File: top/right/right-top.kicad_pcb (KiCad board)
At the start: 2 copper layers, 171 x 95 mm, 39 parts

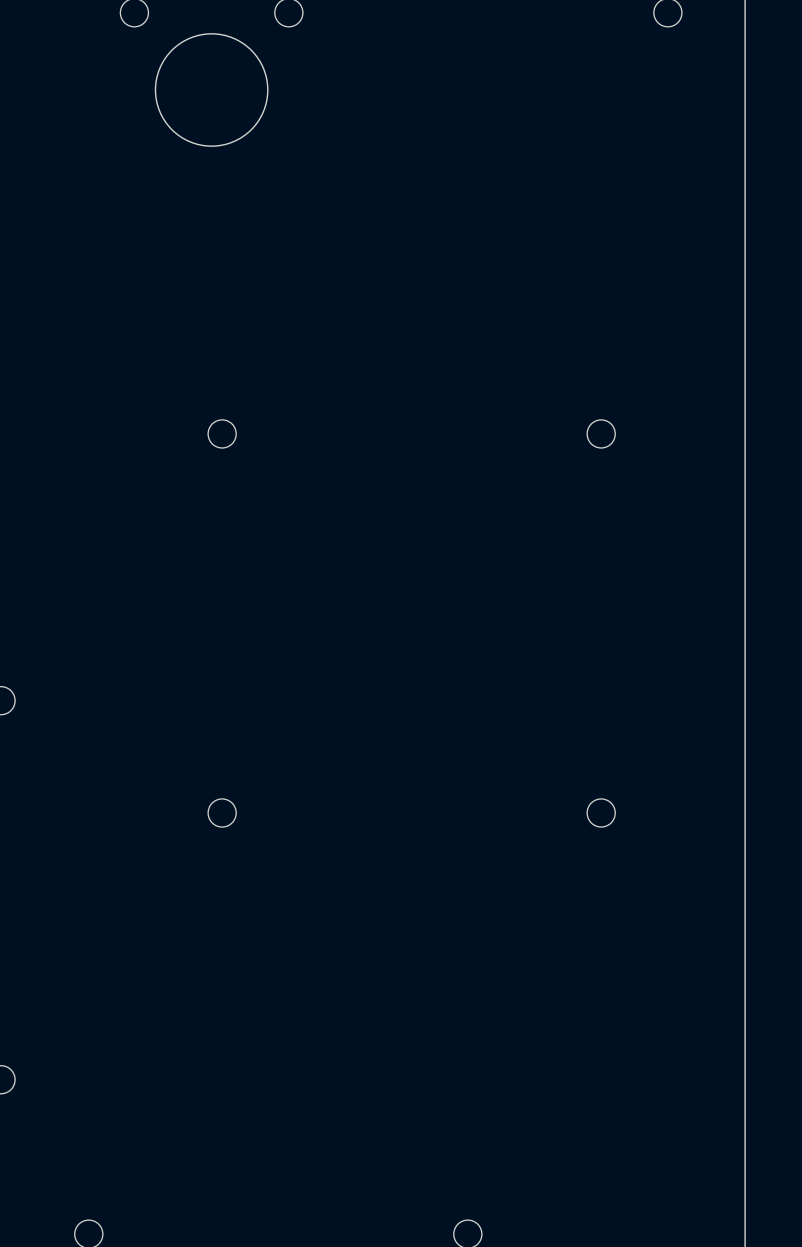
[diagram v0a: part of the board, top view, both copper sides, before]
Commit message: change stabilizer cutout
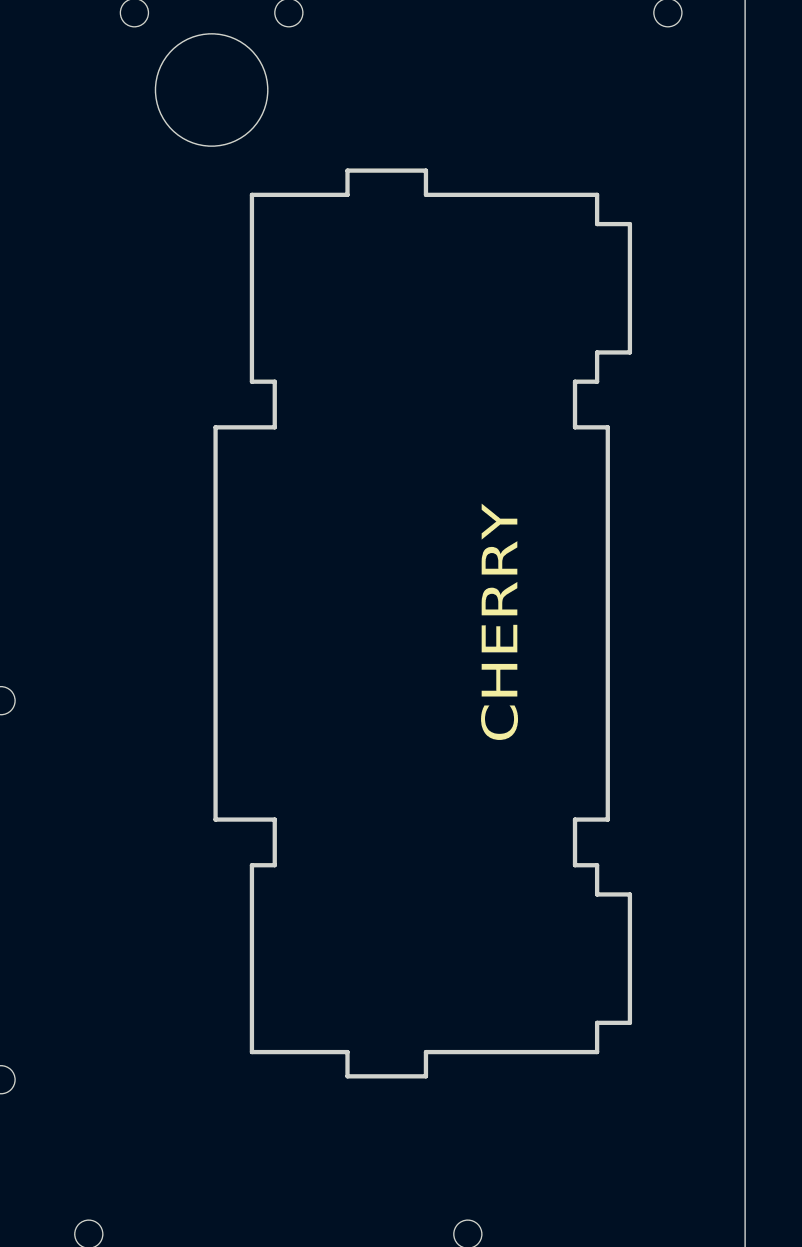
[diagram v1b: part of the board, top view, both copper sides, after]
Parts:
- removed the MX_CUTOUT at (197.1, 83.1)
- removed REF**: MX_Stabilizer_Cutout-2u, Keebio-Parts:MX_Stabilizer_Cutout-2u
- added CHERRY: MX, lib:MX_PCB_CUTOUT, F.Cu at (197.1, 83.1)
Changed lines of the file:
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@@
     (tracks 0)
     (zones 0)
-    (modules 39)
+    (modules 38)
     (nets 1)
   )
@@
     (uvia_drill 0.1)
   )
+  (module lib:MX_PCB_CUTOUT (layer F.Cu)
+    (at 197.125 83.125 90)
+    (fp_text reference CHERRY (at 0 3.175 90) (layer F.SilkS)
+      (effects (font (size 1.27 1.524) (thickness 0.2032)))
+    )
+    (fp_text value MX (at 0 5.08 90) (layer F.SilkS) hide
+      (effects (font (size 1.27 1.524) (thickness 0.2032)))
+    )
+    (fp_circle (center 11.938 8.255) (end 13.938 8.255) (layer Dwgs.User) (width 0.12))
+    (fp_circle (center -11.938 8.255) (end -9.938 8.255) (layer Dwgs.User) (width 0.12))
+    (fp_circle (center -11.938 -6.985) (end -10.438 -6.985) (layer Dwgs.User) (width 0.12))
+    (fp_circle (center 11.938 -6.985) (end 13.438 -6.985) (layer Dwgs.User) (width 0.12))
+    (fp_circle (center 0 0) (end 2 0) (layer Dwgs.User) (width 0.12))
+    (fp_line (start -6.985 -6.985) (end 6.985 -6.985) (layer Edge.Cuts) (width 0.1524))
+    (fp_line (start 6.985 -6.985) (end 6.985 -4.8768) (layer Edge.Cuts) (width 0.1524))
+    (fp_line (start 6.985 -4.8768) (end 8.6106 -4.8768) (layer Edge.Cuts) (width 0.1524))
+    (fp_line (start 8.6106 -4.8768) (end 8.6106 -5.6896) (layer Edge.Cuts) (width 0.1524))
+    (fp_line (start 8.6106 -5.6896) (end 15.2654 -5.6896) (layer Edge.Cuts) (width 0.1524))
+    (fp_line (start 15.2654 -5.6896) (end 15.2654 -2.286) (layer Edge.Cuts) (width 0.1524))
+    (fp_line (start 15.2654 -2.286) (end 16.129 -2.286) (layer Edge.Cuts) (width 0.1524))
+    (fp_line (start 16.129 -2.286) (end 16.129 0.508) (layer Edge.Cuts) (width 0.1524))
+    (fp_line (start 16.129 0.508) (end 15.2654 0.508) (layer Edge.Cuts) (width 0.1524))
+    (fp_line (start 15.2654 0.508) (end 15.2654 6.604) (layer Edge.Cuts) (width 0.1524))
+    (fp_line (start 15.2654 6.604) (end 14.224 6.604) (layer Edge.Cuts) (width 0.1524))
+    (fp_line (start 14.224 6.604) (end 14.224 7.7724) (layer Edge.Cuts) (width 0.1524))
+    (fp_line (start 14.224 7.7724) (end 9.652 7.7724) (layer Edge.Cuts) (width 0.1524))
+    (fp_line (start 9.652 7.7724) (end 9.652 6.604) (layer Edge.Cuts) (width 0.1524))
+    (fp_line (start 9.652 6.604) (end 8.6106 6.604) (layer Edge.Cuts) (width 0.1524))
+    (fp_line (start 8.6106 6.604) (end 8.6106 5.8166) (layer Edge.Cuts) (width 0.1524))
+    (fp_line (start 8.6106 5.8166) (end 6.985 5.8166) (layer Edge.Cuts) (width 0.1524))
+    (fp_line (start 6.985 5.8166) (end 6.985 6.985) (layer Edge.Cuts) (width 0.1524))
+    (fp_line (start 6.985 6.985) (end -6.985 6.985) (layer Edge.Cuts) (width 0.1524))
+    (fp_line (start -6.985 6.985) (end -6.985 5.8166) (layer Edge.Cuts) (width 0.1524))
+    (fp_line (start -6.985 5.8166) (end -8.6106 5.8166) (layer Edge.Cuts) (width 0.1524))
+    (fp_line (start -8.6106 5.8166) (end -8.6106 6.604) (layer Edge.Cuts) (width 0.1524))
+    (fp_line (start -8.6106 6.604) (end -9.652 6.604) (layer Edge.Cuts) (width 0.1524))
+    (fp_line (start -9.652 6.604) (end -9.652 7.7724) (layer Edge.Cuts) (width 0.1524))
+    (fp_line (start -9.652 7.7724) (end -14.224 7.7724) (layer Edge.Cuts) (width 0.1524))
+    (fp_line (start -14.224 7.7724) (end -14.224 6.604) (layer Edge.Cuts) (width 0.1524))
+    (fp_line (start -14.224 6.604) (end -15.2654 6.604) (layer Edge.Cuts) (width 0.1524))
+    (fp_line (start -15.2654 6.604) (end -15.2654 0.508) (layer Edge.Cuts) (width 0.1524))
+    (fp_line (start -15.2654 0.508) (end -16.129 0.508) (layer Edge.Cuts) (width 0.1524))
+    (fp_line (start -16.129 0.508) (end -16.129 -2.286) (layer Edge.Cuts) (width 0.1524))
+    (fp_line (start -16.129 -2.286) (end -15.2654 -2.286) (layer Edge.Cuts) (width 0.1524))
+    (fp_line (start -15.2654 -2.286) (end -15.2654 -5.6896) (layer Edge.Cuts) (width 0.1524))
+    (fp_line (start -15.2654 -5.6896) (end -8.6106 -5.6896) (layer Edge.Cuts) (width 0.1524))
+    (fp_line (start -8.6106 -5.6896) (end -8.6106 -4.8768) (layer Edge.Cuts) (width 0.1524))
+    (fp_line (start -8.6106 -4.8768) (end -6.985 -4.8768) (layer Edge.Cuts) (width 0.1524))
+    (fp_line (start -6.985 -4.8768) (end -6.985 -6.985) (layer Edge.Cuts) (width 0.1524))
+    (fp_line (start 15.367 -7.62) (end 8.509 -7.62) (layer Cmts.User) (width 0.1524))
+    (fp_line (start 8.509 -7.62) (end 8.509 7.62) (layer Cmts.User) (width 0.1524))
+    (fp_line (start 8.509 7.62) (end -8.509 7.62) (layer Cmts.User) (width 0.1524))
+    (fp_line (start -8.509 7.62) (end -8.509 -7.62) (layer Cmts.User) (width 0.1524))
+    (fp_line (start -8.509 -7.62) (end -15.367 -7.62) (layer Cmts.User) (width 0.1524))
+    (fp_line (start -15.367 -7.62) (end -15.367 10.16) (layer Cmts.User) (width 0.1524))
+    (fp_line (start -15.367 10.16) (end 15.367 10.16) (layer Cmts.User) (width 0.1524))
+    (fp_line (start 15.367 10.16) (end 15.367 -7.62) (layer Cmts.User) (width 0.1524))
+  )
   (module lib:MX_CUTOUT_min_dril_1mm (layer F.Cu)
     (at 66.5 130.625)
@@
     (pad "" np_thru_hole circle (at -6.75 -6.75) (size 1 1) (drill 1) (layers *.Cu *.Mask))
   )
-  (module lib:MX_CUTOUT_min_dril_1mm (layer F.Cu)
-    (at 197.125 83.125)
-    (fp_text reference MX_CUTOUT (at 0 1.5) (layer F.SilkS) hide
-      (effects (font (size 1 1) (thickness 0.15)))
-    )
-    (fp_text value VAL** (at 0 0) (layer F.SilkS) hide
-      (effects (font (size 1 1) (thickness 0.15)))
-    )
-    (fp_line (start -7 -7) (end 7 -7) (layer Dwgs.User) (width 0.12))
-    (fp_line (start 7 -7) (end 7 7) (layer Dwgs.User) (width 0.12))
-    (fp_line (start 7 7) (end -7 7) (layer Dwgs.User) (width 0.12))
-    (fp_line (start -7 7) (end -7 -7) (layer Dwgs.User) (width 0.12))
-    (pad "" np_thru_hole circle (at -6.75 -6.75) (size 1 1) (drill 1) (layers *.Cu *.Mask))
-    (pad "" np_thru_hole circle (at 6.75 -6.75) (size 1 1) (drill 1) (layers *.Cu *.Mask))
-    (pad "" np_thru_hole circle (at 6.75 6.75) (size 1 1) (drill 1) (layers *.Cu *.Mask))
-    (pad "" np_thru_hole circle (at -6.75 6.75) (size 1 1) (drill 1) (layers *.Cu *.Mask))
-    (pad "" np_thru_hole oval (at 0 -6.5) (size 14 1) (drill oval 14 1) (layers *.Cu *.Mask))
-    (pad "" np_thru_hole oval (at 0 6.5) (size 14 1) (drill oval 14 1) (layers *.Cu *.Mask))
-    (pad "" np_thru_hole oval (at -6.5 0 90) (size 14 1) (drill oval 14 1) (layers *.Cu *.Mask))
-    (pad "" np_thru_hole oval (at 6.5 0 90) (size 14 1) (drill oval 14 1) (layers *.Cu *.Mask))
-  )
-  (module Keebio-Parts:MX_Stabilizer_Cutout-2u (layer F.Cu)
-    (at 197.125 83.125 90)
-    (fp_text reference REF** (at 0.25 10.05 90) (layer Eco2.User) hide
-      (effects (font (size 1 1) (thickness 0.15)))
-    )
-    (fp_text value MX_Stabilizer_Cutout-2u (at 0 -15.24 90) (layer F.Fab) hide
-      (effects (font (size 1 1) (thickness 0.15)))
-    )
-    (fp_line (start 19 -9.5) (end 19 9.5) (layer Dwgs.User) (width 0.15))
-    (fp_line (start 19 9.5) (end -19 9.5) (layer Dwgs.User) (width 0.15))
-    (fp_line (start -19 9.5) (end -19 -9.5) (layer Dwgs.User) (width 0.15))
-    (fp_line (start -19 -9.5) (end 19 -9.5) (layer Dwgs.User) (width 0.15))
-    (pad "" np_thru_hole oval (at -11.938 7.7724 90) (size 3.048 0.3048) (drill oval 3.048 0.3048) (layers *.Cu *.Mask))
-    (pad "" np_thru_hole oval (at -10.5664 7.112 90) (size 0.3048 1.4732) (drill oval 0.3048 1.4732) (layers *.Cu *.Mask))
-    (pad "" np_thru_hole oval (at -13.3096 7.112 90) (size 0.3048 1.4732) (drill oval 0.3048 1.4732) (layers *.Cu *.Mask))
-    (pad "" np_thru_hole oval (at -15.5448 0.3556 90) (size 1.1684 0.3048) (drill oval 1.1684 0.3048) (layers *.Cu *.Mask))
-    (pad "" np_thru_hole oval (at -11.938 6.4516 90) (size 6.6548 0.3048) (drill oval 6.6548 0.3048) (layers *.Cu *.Mask))
-    (pad "" np_thru_hole oval (at -8.763 0.4572 90) (size 0.3048 12.2936) (drill oval 0.3048 12.2936) (layers *.Cu *.Mask))
-    (pad "" np_thru_hole oval (at -15.113 0.4572 90) (size 0.3048 12.2936) (drill oval 0.3048 12.2936) (layers *.Cu *.Mask))
-    (pad "" np_thru_hole oval (at -15.9766 -0.889 90) (size 0.3048 2.794) (drill oval 0.3048 2.794) (layers *.Cu *.Mask))
-    (pad "" np_thru_hole oval (at -15.5448 -2.1336 90) (size 1.1684 0.3048) (drill oval 1.1684 0.3048) (layers *.Cu *.Mask))
-    (pad "" np_thru_hole oval (at -11.938 -5.5372 90) (size 6.6548 0.3048) (drill oval 6.6548 0.3048) (layers *.Cu *.Mask))
-    (pad "" np_thru_hole oval (at 15.5448 0.3556 90) (size 1.1684 0.3048) (drill oval 1.1684 0.3048) (layers *.Cu *.Mask))
-    (pad "" np_thru_hole oval (at 13.3096 7.112 90) (size 0.3048 1.4732) (drill oval 0.3048 1.4732) (layers *.Cu *.Mask))
-    (pad "" np_thru_hole oval (at 15.5448 -2.1336 90) (size 1.1684 0.3048) (drill oval 1.1684 0.3048) (layers *.Cu *.Mask))
-    (pad "" np_thru_hole oval (at 10.5664 7.112 90) (size 0.3048 1.4732) (drill oval 0.3048 1.4732) (layers *.Cu *.Mask))
-    (pad "" np_thru_hole oval (at 15.9766 -0.889 90) (size 0.3048 2.794) (drill oval 0.3048 2.794) (layers *.Cu *.Mask))
-    (pad "" np_thru_hole oval (at 15.113 0.4572 90) (size 0.3048 12.2936) (drill oval 0.3048 12.2936) (layers *.Cu *.Mask))
-    (pad "" np_thru_hole oval (at 11.938 6.4516 90) (size 6.6548 0.3048) (drill oval 6.6548 0.3048) (layers *.Cu *.Mask))
-    (pad "" np_thru_hole oval (at 8.763 0.4572 90) (size 0.3048 12.2936) (drill oval 0.3048 12.2936) (layers *.Cu *.Mask))
-    (pad "" np_thru_hole oval (at 11.938 -5.5372 90) (size 6.6548 0.3048) (drill oval 6.6548 0.3048) (layers *.Cu *.Mask))
-    (pad "" np_thru_hole oval (at 11.938 7.7724 90) (size 3.048 0.3048) (drill oval 3.048 0.3048) (layers *.Cu *.Mask))
-  )
   (gr_circle (center 76 121.125) (end 78 121.125) (layer Edge.Cuts) (width 0.05))

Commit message: move right drillhole
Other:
- outline, holes or cut-outs redrawn
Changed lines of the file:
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@@
   )
   (gr_circle (center 76 121.125) (end 78 121.125) (layer Edge.Cuts) (width 0.05))
-  (gr_circle (center 128.25 121.125) (end 130.25 121.125) (layer Edge.Cuts) (width 0.05))
+  (gr_circle (center 118.75 121.125) (end 120.75 121.125) (layer Edge.Cuts) (width 0.05))
   (gr_circle (center 190 121.125) (end 192 121.125) (layer Edge.Cuts) (width 0.05))
   (gr_circle (center 190 64.125) (end 192 64.125) (layer Edge.Cuts) (width 0.05))

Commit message: move screw holl
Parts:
- removed CHERRY: MX, lib:MX_PCB_CUTOUT
- added MX_CUTOUT: VAL**, lib:MX_CUTOUT, F.Cu at (197.1, 83.1)
- added REF**: MX_Stabilizer_Cutout-2u, Keebio-Parts:MX_Stabilizer_Cutout-2u, F.Cu at (197.1, 83.1)
- added REF**: MountingHole_3.7mm, MountingHole:MountingHole_3.7mm, F.Cu at (185.2, 121.1)
- added REF**: MountingHole_3.7mm, MountingHole:MountingHole_3.7mm, F.Cu at (190.0, 64.1)
- added REF**: MountingHole_3.7mm, MountingHole:MountingHole_3.7mm, F.Cu at (123.5, 64.1)
- added REF**: MountingHole_3.7mm, MountingHole:MountingHole_3.7mm, F.Cu at (57.0, 64.1)
- added REF**: MountingHole_3.7mm, MountingHole:MountingHole_3.7mm, F.Cu at (76.0, 121.1)
- added REF**: MountingHole_3.7mm, MountingHole:MountingHole_3.7mm, F.Cu at (118.8, 121.1)
- MX_CUTOUT (x37): footprint lib:MX_CUTOUT_min_dril_1mm -> lib:MX_CUTOUT
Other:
- outline, holes or cut-outs redrawn
- board text added: "rev.1"
